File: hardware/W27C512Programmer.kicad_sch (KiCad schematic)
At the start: 124 parts, among them J1 CTRL, J2 MSB, J3 LSB, J4 Ext_UART, J5 OLED, J6 VP, J7 SAO, J8 Conn_01x02, Q1 MMBT3904, Q10 MMBT3906, Q11 MMBT3904, Q12 MMBT3906, Q2 MMBT3906, Q3 MMBT3904, Q4 MMBT3904, Q5 MMBT3904, Q6 MMBT3906, Q7 MMBT3906, Q8 MMBT3906, Q9 MMBT3904, SW1 RST, SW2 USR, U1 MIC2288, U2 74HC573, U3 74HC573, U4 74HC573, U5 28/32 pin ROM

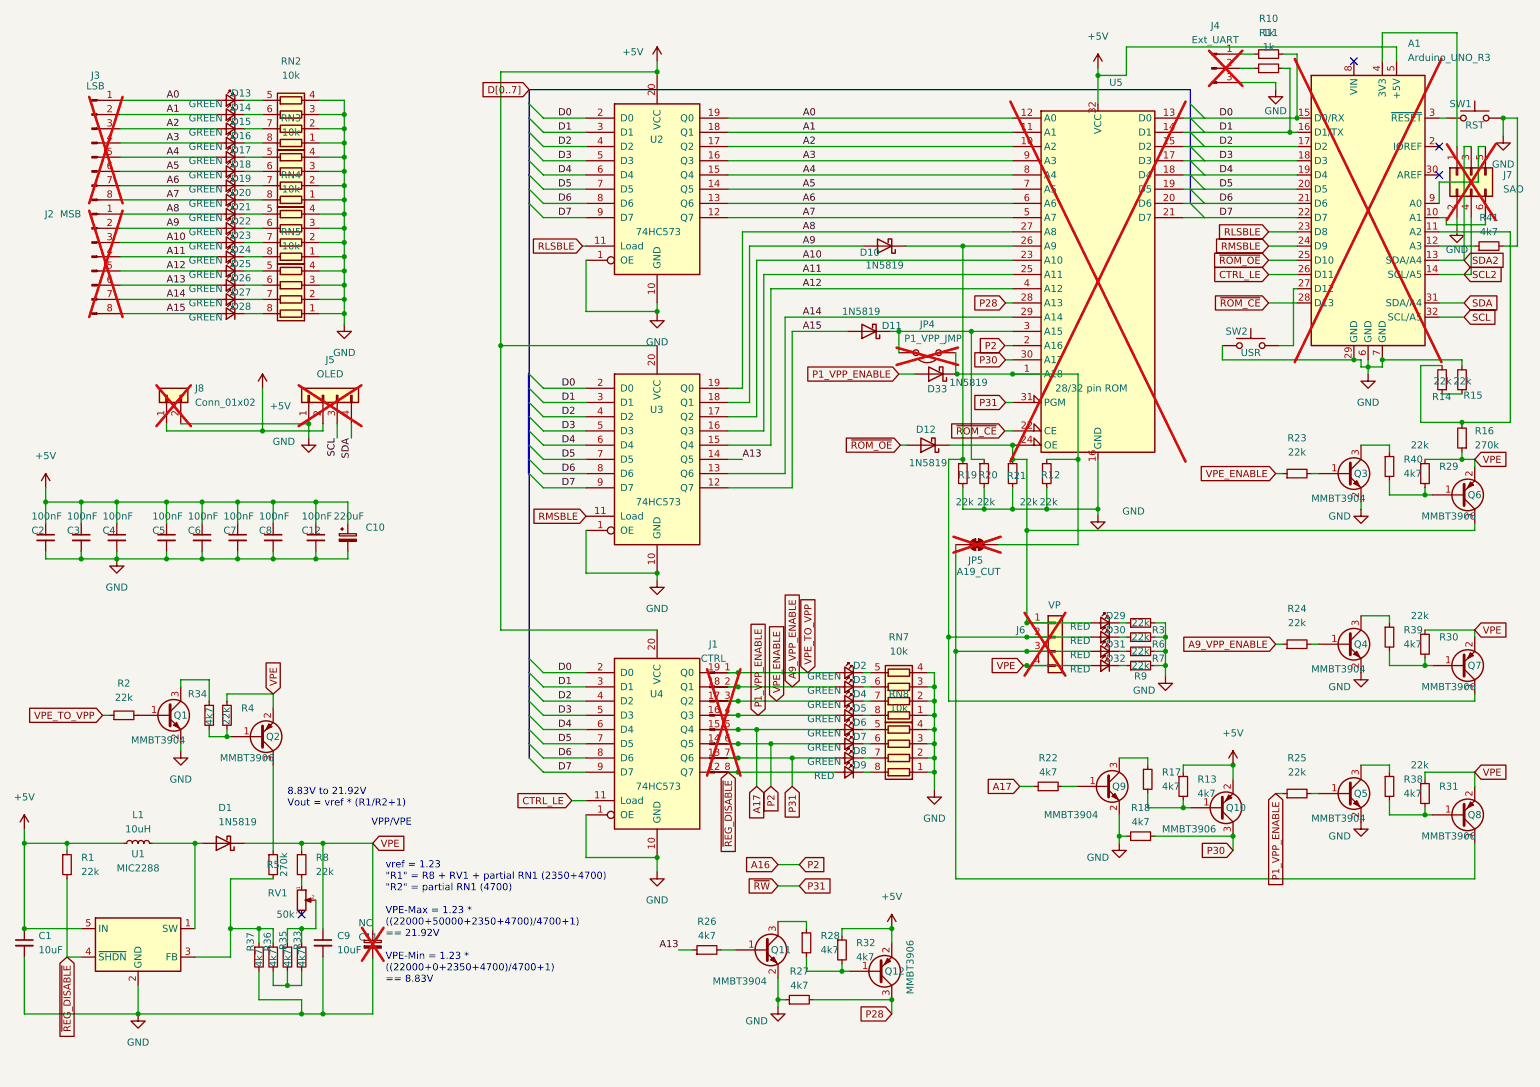
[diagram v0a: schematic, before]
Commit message: U5 changed to a socket part
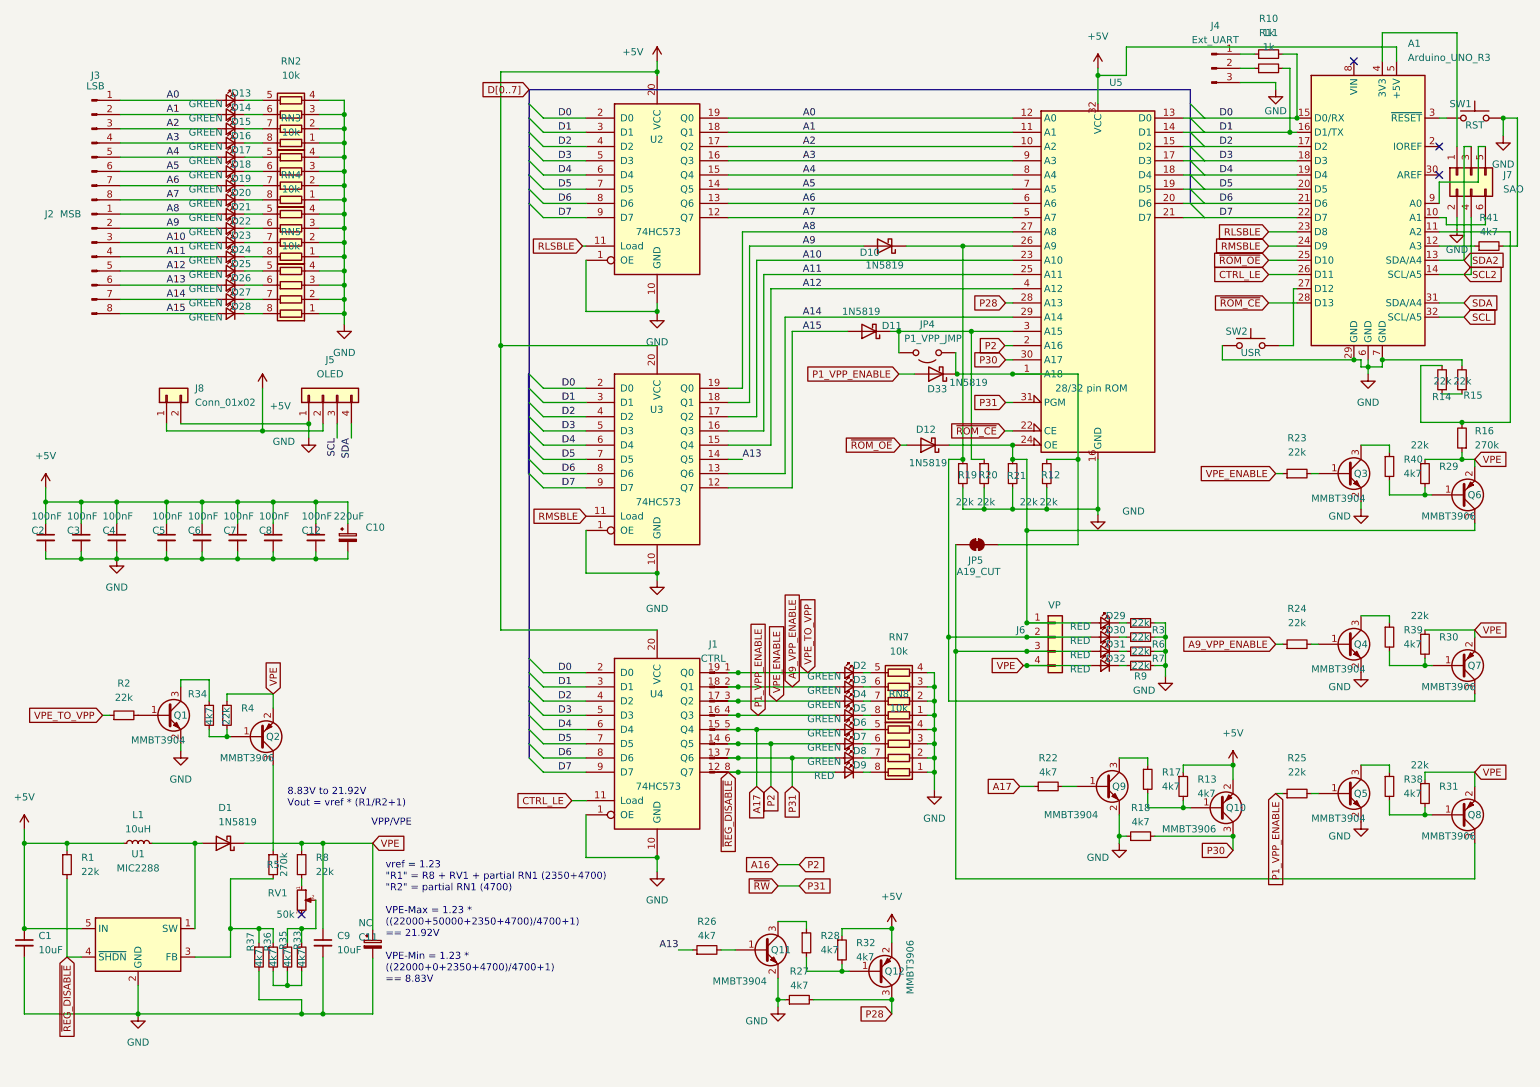
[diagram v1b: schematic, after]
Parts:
- A1, C11, J1, J2, J3, J4, J5, J6, J7, J8, JP4, JP5: now fitted
- U5: LCSC (none) -> C146583; now fitted
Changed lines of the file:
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@@
 		(in_bom yes)
 		(on_board yes)
-		(dnp yes)
+		(dnp no)
 		(property "Reference" "J6"
 			(at 194.945 119.38 0)
@@
 		(in_bom yes)
 		(on_board yes)
-		(dnp yes)
+		(dnp no)
 		(fields_autoplaced yes)
 		(property "Reference" "J7"
@@
 		(in_bom yes)
 		(on_board yes)
-		(dnp yes)
+		(dnp no)
 		(property "Reference" "J2"
 			(at 22.225 45.085 0)
@@
 		(in_bom yes)
 		(on_board yes)
-		(dnp yes)
+		(dnp no)
 		(property "Reference" "J3"
 			(at 30.48 20.32 0)
@@
 		(in_bom yes)
 		(on_board yes)
-		(dnp yes)
+		(dnp no)
 		(fields_autoplaced yes)
 		(property "Reference" "J4"
@@
 		(in_bom yes)
 		(on_board yes)
-		(dnp yes)
+		(dnp no)
 		(fields_autoplaced yes)
 		(property "Reference" "J8"
@@
 		(in_bom yes)
 		(on_board yes)
-		(dnp yes)
+		(dnp no)
 		(fields_autoplaced yes)
 		(property "Reference" "J1"
@@
 		(in_bom yes)
 		(on_board yes)
-		(dnp yes)
+		(dnp no)
 		(property "Reference" "JP4"
 			(at 179.07 64.77 0)
@@
 		(in_bom yes)
 		(on_board yes)
-		(dnp yes)
+		(dnp no)
 		(fields_autoplaced yes)
 		(property "Reference" "J5"
@@
 		(in_bom yes)
 		(on_board yes)
-		(dnp yes)
+		(dnp no)
 		(property "Reference" "U5"
 			(at 211.5694 21.59 0)
@@
 			)
 		)
+		(property "LCSC" "C146583"
+			(at 209.55 58.42 0)
+			(effects
+				(font
+					(size 1.27 1.27)
+				)
+				(hide yes)
+			)
+		)
 		(pin "16"
 		)
@@
 		(in_bom yes)
 		(on_board yes)
-		(dnp yes)
+		(dnp no)
 		(property "Reference" "C11"
 			(at 77.47 174.244 0)
@@
 		(in_bom no)
 		(on_board yes)
-		(dnp yes)
+		(dnp no)
 		(property "Reference" "JP5"
 			(at 187.706 106.934 0)
@@
 		(in_bom no)
 		(on_board yes)
-		(dnp yes)
+		(dnp no)
 		(fields_autoplaced yes)
 		(property "Reference" "A1"
